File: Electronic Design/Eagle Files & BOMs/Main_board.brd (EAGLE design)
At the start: 99.9 x 69 mm, 34 parts, among them IC1 ACS712ELC-5A, IC2 ATMEGA328-PU, Q1 IRF9540, Q2 IRF9540, X1 16MHz

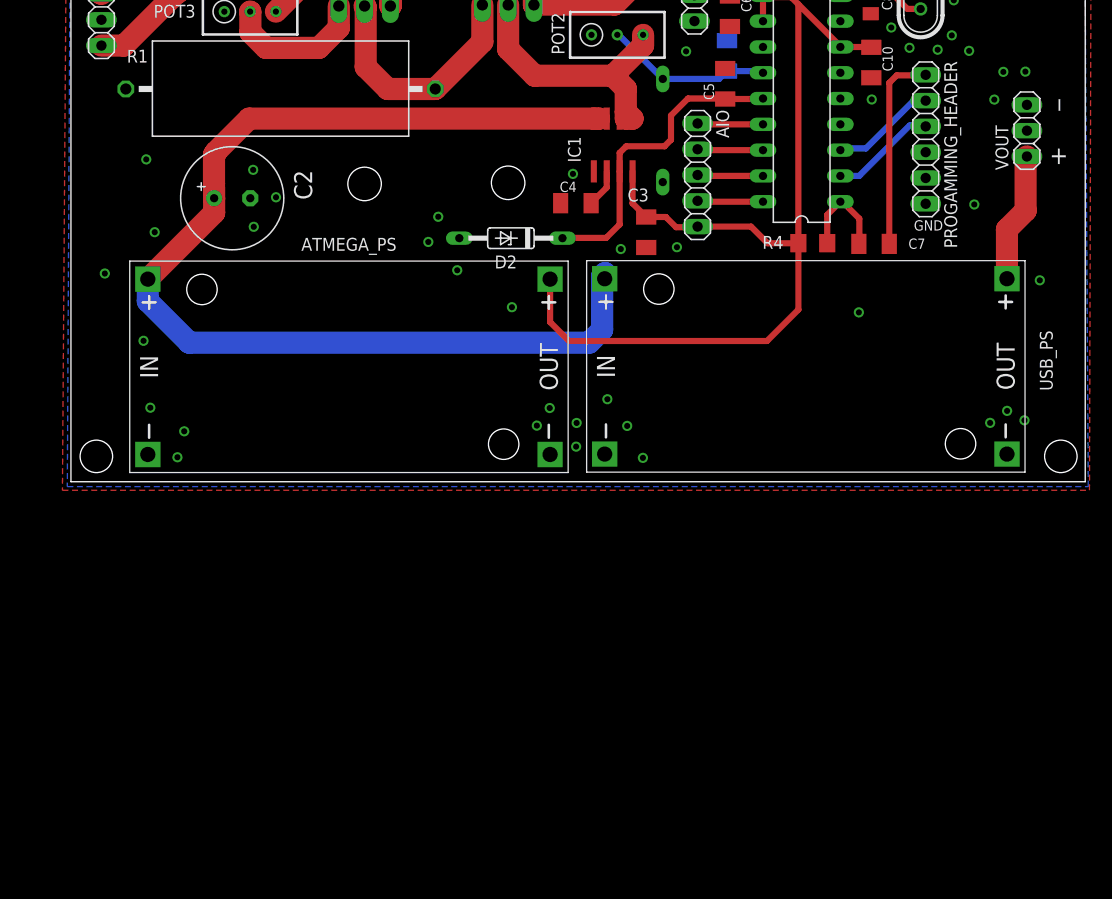
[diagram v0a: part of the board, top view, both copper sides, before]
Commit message: adding new current sensor and buck converter for USB power supply
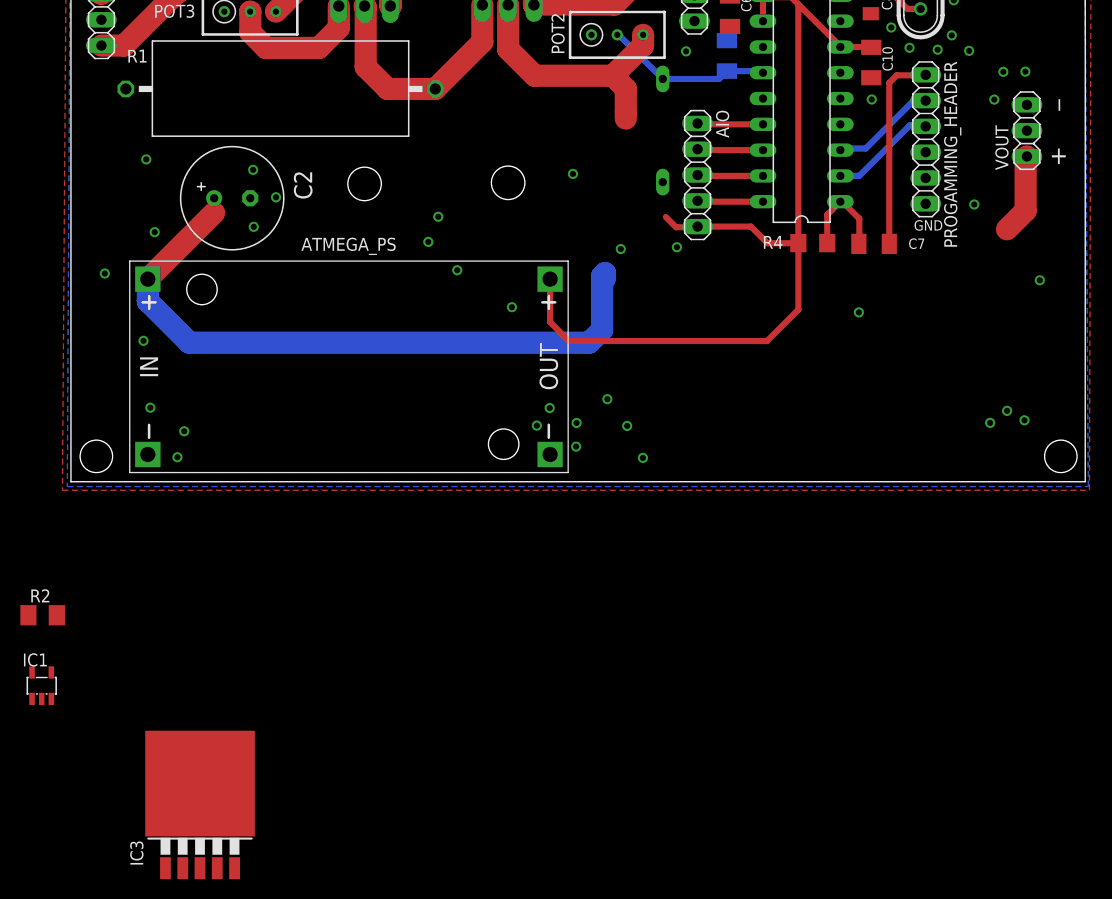
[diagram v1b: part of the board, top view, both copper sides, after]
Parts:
- removed C3, C4: 0.1u, resistor:C1206K
- removed C5: 100pf, resistor:C1206K
- removed D2: 5.1V, diode:DO35Z10
- removed USB_PS: DC-DC-STEP-DOWN-LM2596, diy-modules:DC-DC-STEP-DOWN-LM2596
- added IC3: LM2596S, national-semiconductor:TO263-5
- added R2: (no value), resistor:M1206
- IC1: value ACS712ELC-5A -> MCP73811/2; device mylibrary:SOIC8 -> adafruit:SOT23-5L
- moved IC1 77.5 mm to (-2.88, -20.1), turned to 0 degrees
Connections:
- removed net N$2: C4.2, IC1.6
- net +5V: now also IC1.5; no longer C3.1, IC1.8
- net GND: now also IC1.2, IC3.3, IC3.5; no longer C3.2, C4.1, C5.2, D2.A, IC1.5, USB_PS.IN-, USB_PS.OUT-
- net IIN: now also IC1.1; no longer C5.1, D2.C, IC1.7
- net M1S: now also IC3.1, R2.2; no longer C2.+, IC1.3, USB_PS.IN+
- net N$13: no longer USB_PS.OUT+
- net N$3: now also C2.+, IC1.3, R2.1; no longer IC1.1, IC1.2
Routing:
- net M1S: track 110.6 -> 64.6 mm
- net IIN: track 31.0 -> 0.06 mm
- net +5V: track 128.5 -> 121.5 mm
- net N$13: track 12.9 -> 7.99 mm
- net N$2: track 3.77 -> 0.00 mm
- net N$3: track 28.6 -> 25.8 mm

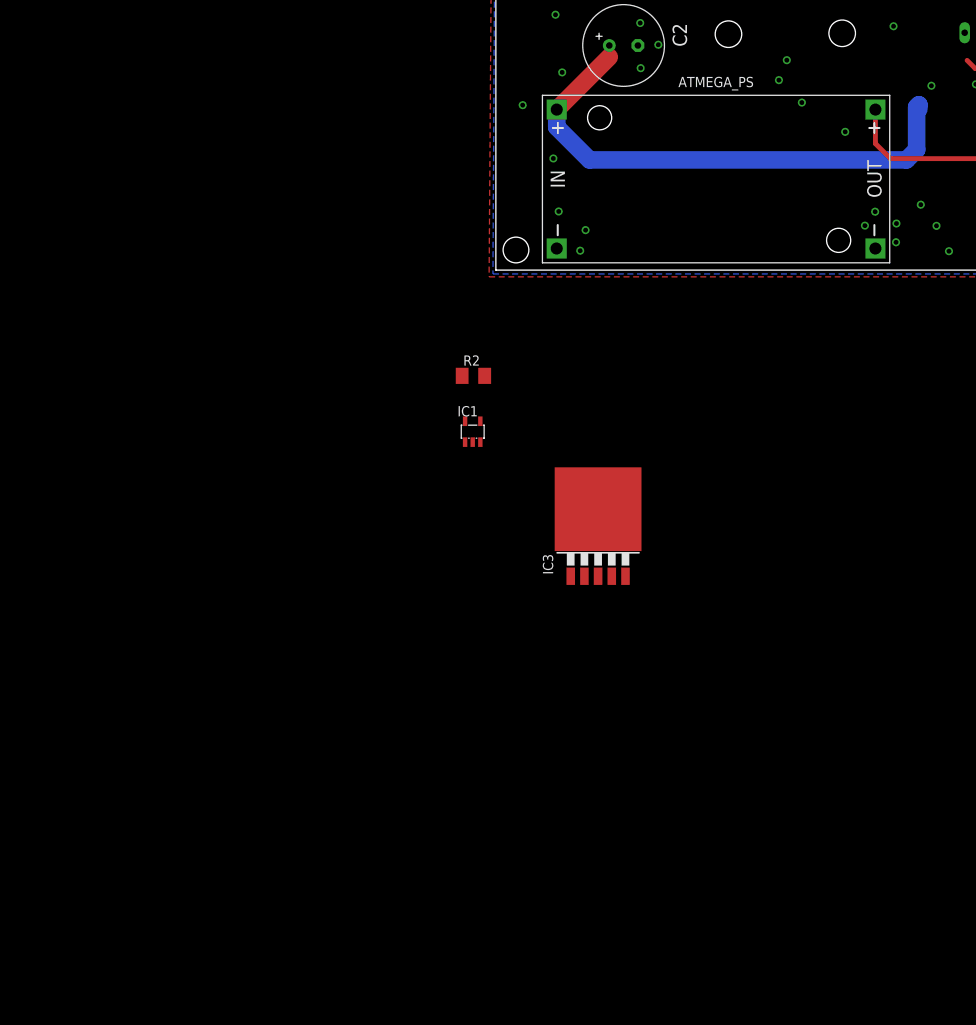
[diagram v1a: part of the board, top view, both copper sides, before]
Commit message: adding new arduino voltage reg and improved schematic symbol for CS30
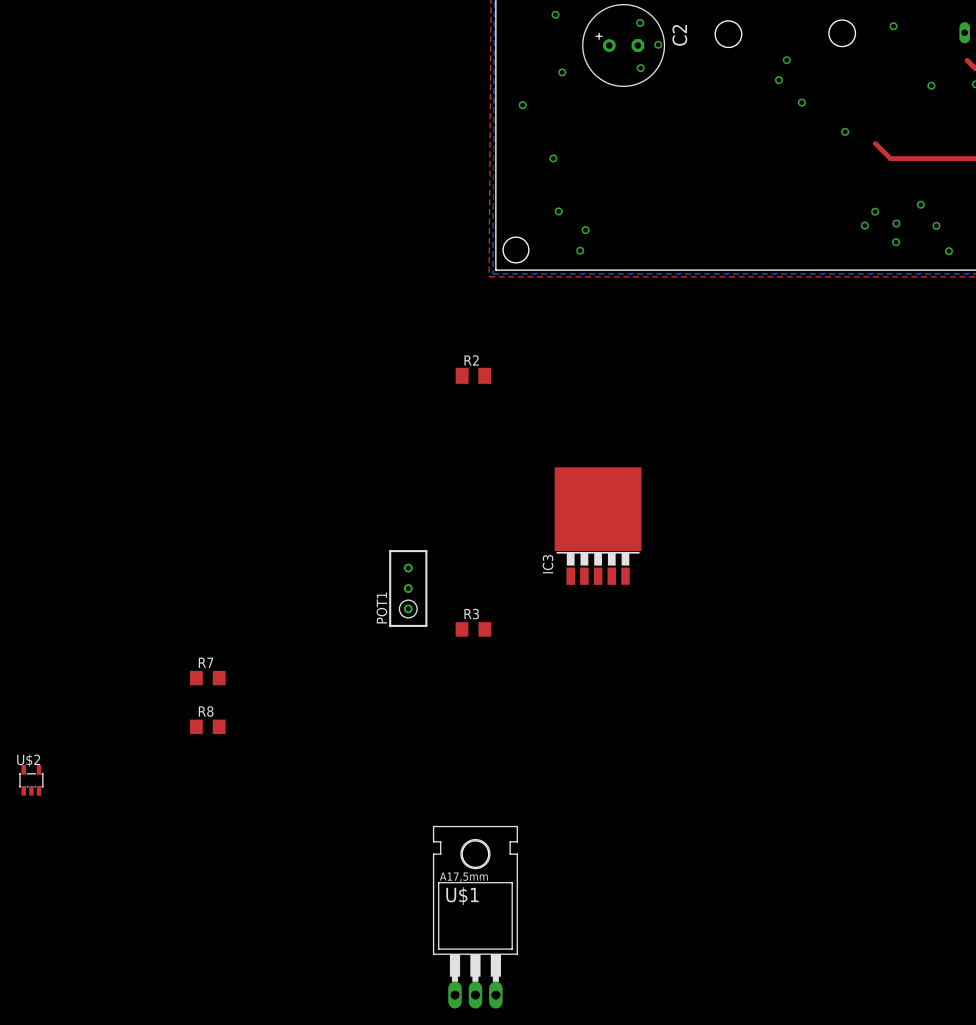
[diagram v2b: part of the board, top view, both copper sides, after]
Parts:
- removed ATMEGA_PS: DC-DC-STEP-DOWN-LM2596, diy-modules:DC-DC-STEP-DOWN-LM2596
- removed IC1: MCP73811/2, adafruit:SOT23-5L
- added POT1: 10k, resistor:RTRIM3296W
- added R3: 2k, resistor:R1206
- added R7: 1k, resistor:R1206
- added R8: 3k, resistor:R1206
- added U$1: LM317, Samson:TO220BH
- added U$2: CS30, Samson:SOT23-5L
- R2: value (none) -> 0R01
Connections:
- new net N$2: IC3.4, POT1.3, R3.2
- new net N$23: R7.1, R8.2, U$1.1
- net +5V: now also R7.2, U$1.2, U$2.5; no longer ATMEGA_PS.OUT+, IC1.5
- net GND: now also R3.1, R8.1, U$2.2; no longer ATMEGA_PS.IN-, ATMEGA_PS.OUT-, IC1.2
- net IIN: now also U$2.1; no longer IC1.1
- net M1S: now also POT1.1, POT1.2, U$1.3, U$2.4; no longer ATMEGA_PS.IN+, IC1.4
- net N$13: now also IC3.2
- net N$3: now also U$2.3; no longer IC1.3
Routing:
- net M1S: track 64.6 -> 0.00 mm
- net +5V: track 121.5 -> 117.3 mm
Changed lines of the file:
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@@
 <attribute name="VALUE" x="93.205" y="49.07" size="1.27" layer="27" rot="R90"/>
 </element>
-<element name="ATMEGA_PS" library="diy-modules" package="DC-DC-STEP-DOWN-LM2596" value="DC-DC-STEP-DOWN-LM2596" x="27.38" y="11.32"/>
 <element name="VOUT" library="pinhead" package="1X03" value="" x="94.16" y="34.58" rot="R90"/>
 <element name="C6" library="resistor" package="C1206K" value="0.1u" x="64.91" y="46.34" rot="R270"/>
 <element name="C10" library="resistor" package="C1206K" value="0.1u" x="78.83" y="41.29" rot="R270"/>
 <element name="AIO" library="pinhead" package="1X05" value="" x="61.72" y="30.21" rot="R270"/>
-<element name="R2" library="resistor" package="M1206" value="" x="-2.79" y="-13.15"/>
-<element name="IC1" library="adafruit" package="SOT23-5L" value="MCP73811/2" x="-2.88" y="-20.09"/>
+<element name="R2" library="resistor" package="M1206" value="0R01" x="-2.79" y="-13.15"/>
 <element name="IC3" library="national-semiconductor" package="TO263-5" value="LM2596S" x="12.71" y="-32.27">
 <attribute name="MF" value="NATIONAL SEMICONDUCTOR" x="12.71" y="-32.27" size="1.778" layer="27" display="off"/>
@@
 <attribute name="MPN" value="LM2596S-ADJ/NOPB" x="12.71" y="-32.27" size="1.778" layer="27" display="off"/>
 </element>
+<element name="R3" library="resistor" package="R1206" value="2k" x="-2.79" y="-44.67"/>
+<element name="POT1" library="resistor" package="RTRIM3296W" value="10k" x="-10.89" y="-39.59"/>
+<element name="R7" library="resistor" package="R1206" value="1k" x="-35.82" y="-50.73"/>
+<element name="R8" library="resistor" package="R1206" value="3k" x="-35.82" y="-56.79"/>
+<element name="U$1" library="Samson" package="TO220BH" value="LM317" x="-2.54" y="-83.79"/>
+<element name="U$2" library="Samson" package="SOT23-5L" value="CS30" x="-57.75" y="-63.44"/>
 </elements>
 <signals>
@@
 <contactref element="IC2" pad="24"/>
 <wire x1="68.119609375" y1="37.7" x2="68.1625375" y2="37.742928125" width="0.6096" layer="1"/>
-<contactref element="IC1" pad="1"/>
-<wire x1="-3.83" y1="-21.39" x2="68.119609375" y2="37.7" width="0" layer="19" extent="1-1"/>
+<contactref element="U$2" pad="1"/>
+<wire x1="68.119609375" y1="37.7" x2="-58.7" y2="-64.74" width="0" layer="19" extent="1-1"/>
 </signal>
 <signal name="GND">
@@
 </polygon>
 <contactref element="DIO_PINS" pad="1"/>
-<contactref element="ATMEGA_PS" pad="IN-"/>
-<contactref element="ATMEGA_PS" pad="OUT-"/>
 <contactref element="VOUT" pad="3"/>
 <contactref element="C10" pad="2"/>
@@
 <contactref element="ATMEGA_DIO" pad="7"/>
 <contactref element="C2" pad="-"/>
-<contactref element="IC1" pad="2"/>
 <contactref element="IC3" pad="3"/>
 <contactref element="IC3" pad="5"/>
+<contactref element="R3" pad="1"/>
+<contactref element="R8" pad="1"/>
+<contactref element="U$2" pad="2"/>
 <wire x1="87.304609375" y1="49.90186875" x2="90.03" y2="49.07" width="0" layer="19" extent="1-1"/>
 <wire x1="86.95569375" y1="47.4202" x2="87.304609375" y2="49.90186875" width="0" layer="19" extent="1-1"/>
@@
 <wire x1="49.80569375" y1="5.7902" x2="47.15569375" y2="7.2602" width="0" layer="19" extent="1-1"/>
 <wire x1="49.75569375" y1="3.4602" x2="49.80569375" y2="5.7902" width="0" layer="19" extent="1-1"/>
-<wire x1="47.192" y1="2.684" x2="49.75569375" y2="3.4602" width="0" layer="19" extent="1-1"/>
 <wire x1="52.83569375" y1="8.1302" x2="49.80569375" y2="5.7902" width="0" layer="19" extent="1-1"/>
 <wire x1="54.78569375" y1="5.5002" x2="52.83569375" y2="8.1302" width="0" layer="19" extent="1-1"/>
@@
 <wire x1="11.15569375" y1="4.9702" x2="7.81569375" y2="7.2902" width="0" layer="19" extent="1-1"/>
 <wire x1="10.48569375" y1="2.4102" x2="11.15569375" y2="4.9702" width="0" layer="19" extent="1-1"/>
-<wire x1="7.568" y1="2.684" x2="10.48569375" y2="2.4102" width="0" layer="19" extent="1-1"/>
 <wire x1="15.105396875" y1="46.30505" x2="5.40296875" y2="38.686728125" width="0" layer="19" extent="1-1"/>
-<wire x1="-2.88" y1="-21.39" x2="7.568" y2="2.684" width="0" layer="19" extent="1-1"/>
-<wire x1="12.71" y1="-38.0612" x2="-2.88" y2="-21.39" width="0" layer="19" extent="1-1"/>
+<wire x1="12.71" y1="-38.0612" x2="10.48569375" y2="2.4102" width="0" layer="19" extent="1-1"/>
 <wire x1="16.1136" y1="-38.0612" x2="12.71" y2="-38.0612" width="0" layer="19" extent="1-1"/>
+<wire x1="-4.212" y1="-44.67" x2="12.71" y2="-38.0612" width="0" layer="19" extent="1-1"/>
+<wire x1="-37.242" y1="-56.79" x2="-4.212" y2="-44.67" width="0" layer="19" extent="1-1"/>
+<wire x1="-57.75" y1="-64.74" x2="-37.242" y2="-56.79" width="0" layer="19" extent="1-1"/>
 </signal>
 <signal name="M1S">
-<contactref element="ATMEGA_PS" pad="IN+"/>
-<wire x1="7.568" y1="19.956" x2="7.568" y2="17.782" width="2.1844" layer="16"/>
-<wire x1="7.568" y1="17.782" x2="11.65" y2="13.7" width="2.1844" layer="16"/>
-<wire x1="11.65" y1="13.7" x2="51.05" y2="13.7" width="2.1844" layer="16"/>
-<wire x1="51.05" y1="13.7" x2="52.32" y2="14.97" width="2.1844" layer="16"/>
-<wire x1="52.32" y1="14.97" x2="52.32" y2="20.27" width="2.1844" layer="16"/>
-<wire x1="52.32" y1="20.27" x2="52.6" y2="20.55" width="2.1844" layer="16"/>
-<wire x1="52.6" y1="20.55" x2="52.6" y2="20.028" width="2.1844" layer="16"/>
-<wire x1="14.103284375" y1="26.491284375" x2="7.568" y2="19.956" width="2.1844" layer="1"/>
 <contactref element="R2" pad="2"/>
-<contactref element="IC1" pad="4"/>
 <contactref element="IC3" pad="1"/>
-<wire x1="-1.93" y1="-18.79" x2="9.3064" y2="-38.0612" width="0" layer="19" extent="1-1"/>
-<wire x1="-1.39" y1="-13.15" x2="-1.93" y2="-18.79" width="0" layer="19" extent="1-1"/>
-<wire x1="11.65" y1="13.7" x2="-1.39" y2="-13.15" width="0" layer="19" extent="1-16"/>
+<contactref element="POT1" pad="1"/>
+<contactref element="POT1" pad="2"/>
+<contactref element="U$1" pad="3"/>
+<contactref element="U$2" pad="4"/>
+<wire x1="0" y1="-90.14" x2="-56.8" y2="-62.14" width="0" layer="19" extent="1-1"/>
+<wire x1="-10.89" y1="-42.13" x2="0" y2="-90.14" width="0" layer="19" extent="1-1"/>
+<wire x1="-10.89" y1="-39.59" x2="-10.89" y2="-42.13" width="0" layer="19" extent="1-1"/>
+<wire x1="9.3064" y1="-38.0612" x2="-10.89" y2="-39.59" width="0" layer="19" extent="1-1"/>
+<wire x1="-1.39" y1="-13.15" x2="9.3064" y2="-38.0612" width="0" layer="19" extent="1-1"/>
 </signal>
 <signal name="N$3">
@@
 <contactref element="C2" pad="+"/>
 <contactref element="R2" pad="1"/>
-<contactref element="IC1" pad="3"/>
-<wire x1="14.103284375" y1="27.927296875" x2="43.060084375" y2="42.609915625" width="0" layer="19" extent="1-1"/>
-<wire x1="-4.19" y1="-13.15" x2="14.103284375" y2="27.927296875" width="0" layer="19" extent="1-1"/>
-<wire x1="-1.93" y1="-21.39" x2="-4.19" y2="-13.15" width="0" layer="19" extent="1-1"/>
+<contactref element="U$2" pad="3"/>
+<wire x1="-4.19" y1="-13.15" x2="-56.8" y2="-64.74" width="0" layer="19" extent="1-1"/>
+<wire x1="14.103284375" y1="27.927296875" x2="-4.19" y2="-13.15" width="0" layer="19" extent="1-1"/>
+<wire x1="43.060084375" y1="42.609915625" x2="14.103284375" y2="27.927296875" width="0" layer="19" extent="1-1"/>
 </signal>
 <signal name="N$10">
@@
 <wire x1="71.64436875" y1="47.02563125" x2="70.94" y2="47.73" width="0.6096" layer="1"/>
 <wire x1="71.64436875" y1="23.501790625" x2="71.65" y2="23.496159375" width="0.6096" layer="1"/>
-<contactref element="ATMEGA_PS" pad="OUT+"/>
-<wire x1="47.192" y1="19.956" x2="47.192" y2="15.728" width="0.6096" layer="1"/>
 <wire x1="47.192" y1="15.728" x2="49.06" y2="13.86" width="0.6096" layer="1"/>
 <wire x1="68.56" y1="13.86" x2="49.06" y2="13.86" width="0.6096" layer="1"/>
@@
 <wire x1="68.62" y1="23.49" x2="71.632578125" y2="23.49" width="0.6096" layer="1"/>
 <wire x1="71.632578125" y1="23.49" x2="71.64436875" y2="23.501790625" width="0.6096" layer="1"/>
-<contactref element="IC1" pad="5"/>
-<wire x1="-3.83" y1="-18.79" x2="47.192" y2="15.728" width="0" layer="19" extent="1-1"/>
+<contactref element="R7" pad="2"/>
+<contactref element="U$1" pad="2"/>
+<contactref element="U$2" pad="5"/>
+<wire x1="-2.54" y1="-90.14" x2="-58.7" y2="-62.14" width="0" layer="19" extent="1-1"/>
+<wire x1="-34.398" y1="-50.73" x2="-2.54" y2="-90.14" width="0" layer="19" extent="1-1"/>
+<wire x1="47.192" y1="15.728" x2="-34.398" y2="-50.73" width="0" layer="19" extent="1-1"/>
 </signal>
 <signal name="N$15">
@@
 <wire x1="94.03" y1="26.7" x2="94.03" y2="31.91" width="2.1844" layer="1"/>
 <wire x1="94.03" y1="31.91" x2="94.16" y2="32.04" width="2.1844" layer="1"/>
+<contactref element="IC3" pad="2"/>
+<wire x1="11.0082" y1="-38.0612" x2="92.192" y2="24.862" width="0" layer="19" extent="1-1"/>
 </signal>
 <signal name="ANALOG_4">
@@
 <wire x1="61.812928125" y1="27.582928125" x2="61.72" y2="27.67" width="0.6096" layer="1"/>
 </signal>
+<signal name="N$2">
+<contactref element="IC3" pad="4"/>
+<contactref element="R3" pad="2"/>
+<contactref element="POT1" pad="3"/>
+<wire x1="-1.368" y1="-44.67" x2="-10.89" y2="-37.05" width="0" layer="19" extent="1-1"/>
+<wire x1="14.4118" y1="-38.0612" x2="-1.368" y2="-44.67" width="0" layer="19" extent="1-1"/>
+</signal>
+<signal name="N$23">
+<contactref element="R7" pad="1"/>
+<contactref element="R8" pad="2"/>
+<contactref element="U$1" pad="1"/>
+<wire x1="-37.242" y1="-50.73" x2="-5.08" y2="-90.14" width="0" layer="19" extent="1-1"/>
+<wire x1="-34.398" y1="-56.79" x2="-37.242" y2="-50.73" width="0" layer="19" extent="1-1"/>
+</signal>
 </signals>
